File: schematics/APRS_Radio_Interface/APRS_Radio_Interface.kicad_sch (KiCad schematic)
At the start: 24 parts, among them J1 TRS 2.5mm, J2 TS 3.5mm, Q1 2N2222, U1 PC817

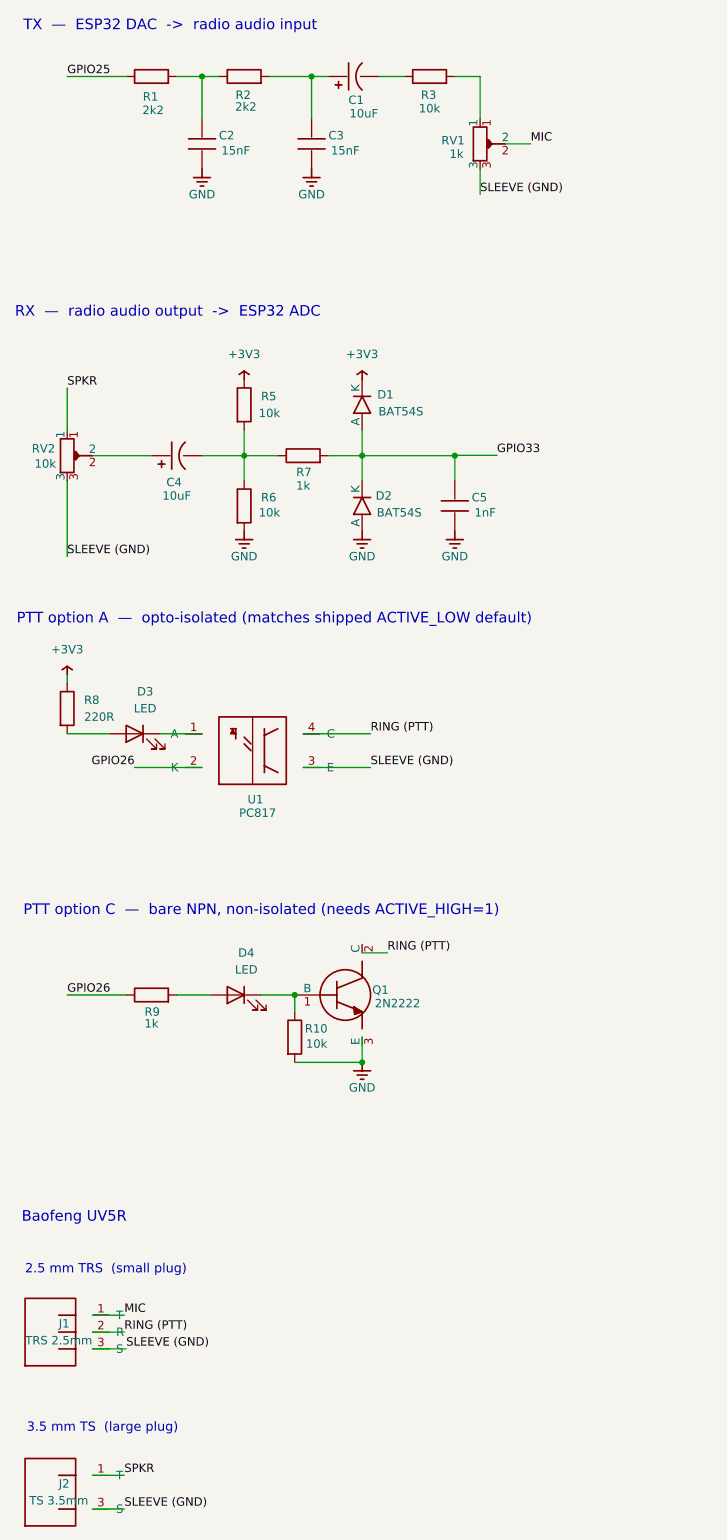
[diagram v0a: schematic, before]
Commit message: Add APRS Coverage docs
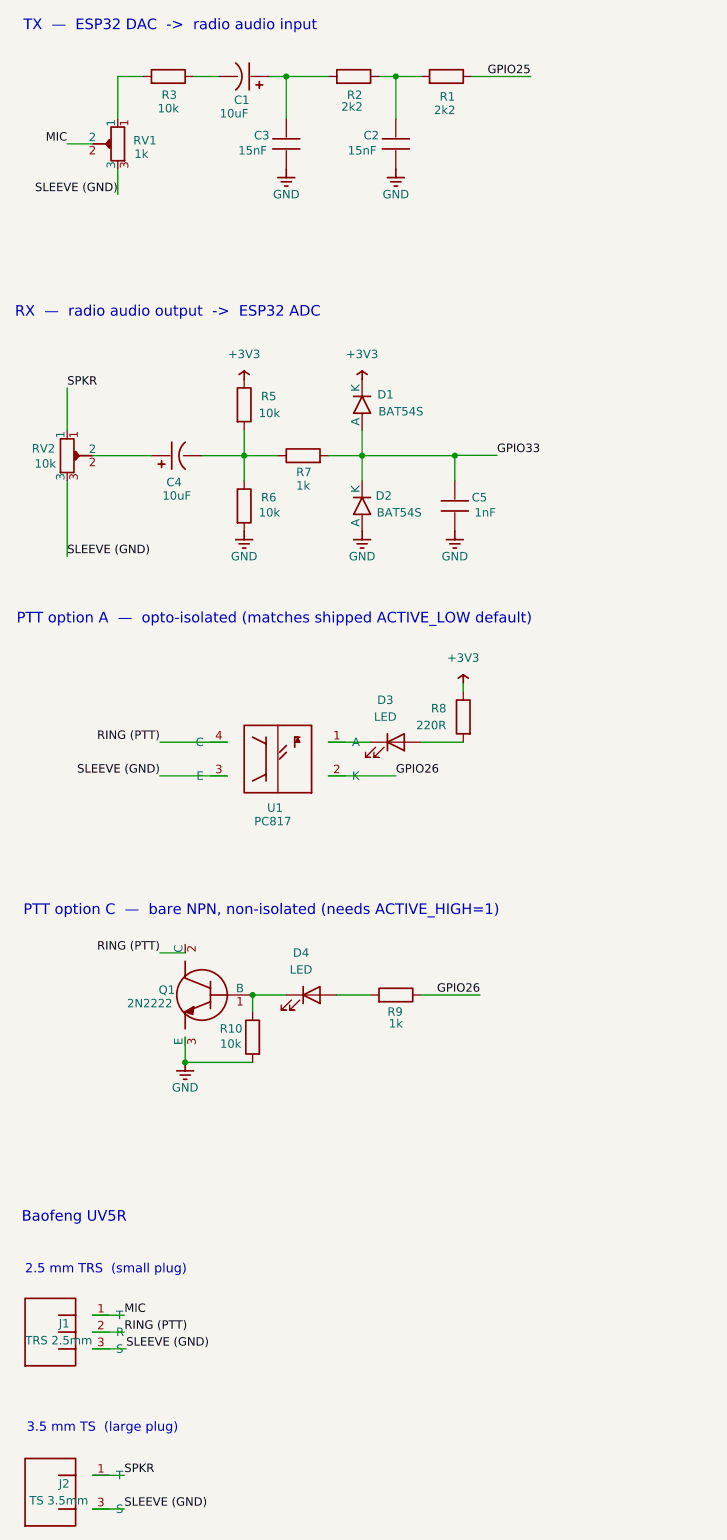
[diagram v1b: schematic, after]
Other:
- moved on the sheet: C1, C2, C3, D3, D4, Q1, R1, R10, R2, R3, R8, R9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
